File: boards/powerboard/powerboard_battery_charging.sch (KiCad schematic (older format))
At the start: 19 parts, among them P501 10k NTC, Q501 DMN6140L, Q502 PMV27UPE, Q503 IRF7343PBF, U501 LTC4010

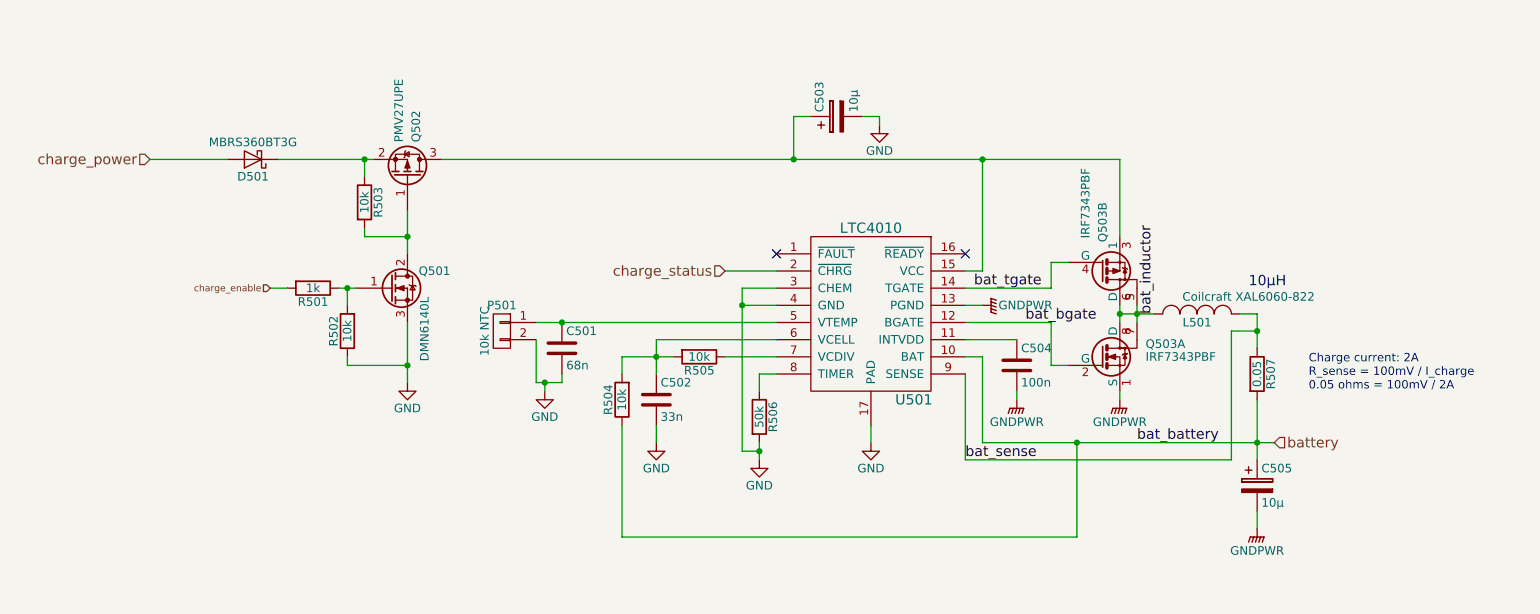
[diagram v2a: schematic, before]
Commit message: [powerboard] improve LTC4010
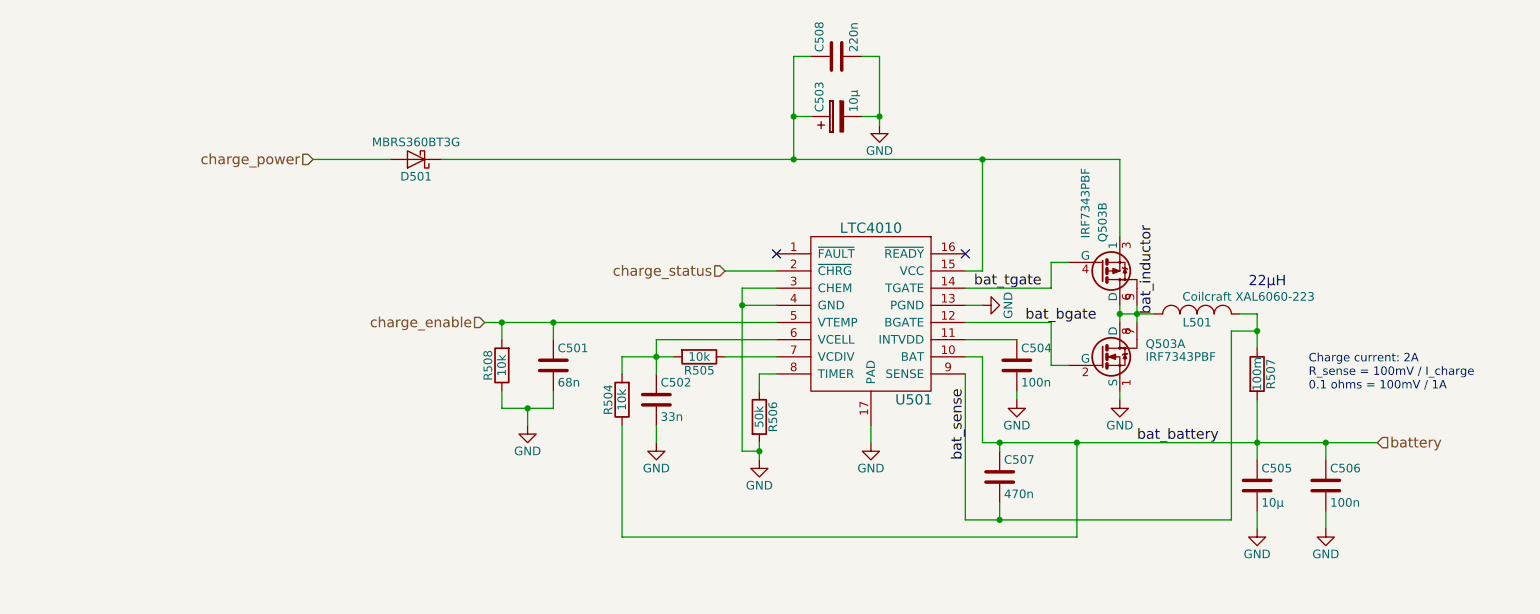
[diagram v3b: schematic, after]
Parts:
- removed C505: 10µ, Capacitors_SMD:C_0805, symbol CP
- removed P501: 10k NTC, Pin_Headers:Pin_Header_Straight_1x02_Pitch2.54mm, symbol CONN_01X02
- removed Q501: DMN6140L, TO_SOT_Packages_SMD:SOT-23, symbol Q_NMOS_GDS
- removed Q502: PMV27UPE, TO_SOT_Packages_SMD:SOT-23, symbol Q_PMOS_GSD
- removed R501: 1k, Resistors_SMD:R_0603, symbol R
- removed R502, R503: 10k, Resistors_SMD:R_0603, symbol R
- added C505: 10µ, symbol C
- added C506: 100n, symbol C
- added C507: 470n, symbol C
- added C508: 220n, symbol C
- added R508: 10k, Resistors_SMD:R_0603, symbol R
- L501: value Coilcraft XAL6060-822 -> Coilcraft XAL6060-223
- R507: value 0.05 -> 100m
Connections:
- net GNDPWR is gone; now on net GND: C504.2, Q503.1 (S), U501.13 (PGND)
- net GND: now also C505.2, C506.2, C508.2, R508.1
- net bat_sense: now also C507.2
- net battery: now also C505.1, C506.1, C507.1
- net charge_enable: now also C501.1, U501.5 (VTEMP), R508.2
- net at C503.1, Q503.3 (1), U501.15 (VCC): now also D501.1 (K), C508.1
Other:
- note added: "22µH"
- note added: "Charge current: 2A\nR_sense = 100mV / I_charge\n0.1 ohms = 100mV / 1A"
- note removed: "10µH"
- note removed: "Charge current: 2A\nR_sense = 100mV / I_charge\n0.05 ohms = 100mV / 2A"
- moved on the sheet: C501, D501

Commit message: [powerboard] LTC4010: fix R and C values
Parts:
- C502: value 33n -> 47n
- R504: value 10k -> 65k7
- R505: value 10k -> 8k2
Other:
- note added: "9 cells: R504 = 65.7k, R505 = 8.2k, R504/R505 = 8.01\n8 cells: R504 = 57.6k, R505 = 8.2k, R504/R505 = 7.02"
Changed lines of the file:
@@
 P 4950 3750
 F 0 "R505" V 5030 3750 50  0000 C CNN
-F 1 "10k" V 4950 3750 50  0000 C CNN
+F 1 "8k2" V 4950 3750 50  0000 C CNN
 F 2 "Resistors_SMD:R_0603" V 4880 3750 50  0001 C CNN
 F 3 "" H 4950 3750 50  0000 C CNN
@@
 P 4700 4000
 F 0 "C502" H 4725 4100 50  0000 L CNN
-F 1 "33n" H 4725 3900 50  0000 L CNN
+F 1 "47n" H 4725 3900 50  0000 L CNN
 F 2 "Capacitors_SMD:C_0603" H 4738 3850 50  0001 C CNN
 F 3 "" H 4700 4000 50  0000 C CNN
@@
 P 4500 4000
 F 0 "R504" V 4580 4000 50  0000 C CNN
-F 1 "10k" V 4500 4000 50  0000 C CNN
+F 1 "65k7" V 4500 4000 50  0000 C CNN
 F 2 "Resistors_SMD:R_0603" V 4430 4000 50  0001 C CNN
 F 3 "" H 4500 4000 50  0000 C CNN
@@
 	1    0    0    -1
 $EndComp
+Text Notes 4000 5150 0    60   ~ 0
+9 cells: R504 = 65.7k, R505 = 8.2k, R504/R505 = 8.01\n8 cells: R504 = 57.6k, R505 = 8.2k, R504/R505 = 7.02
 $EndSCHEMATC

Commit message: [powerboard] fix minor issues in all schematics; revision: rev10
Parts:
- C503: value 10µ -> 10µ 0805 35V
- C505: footprint (none) -> Capacitors_SMD:C_0805
- C506, C507, C508: footprint (none) -> Capacitors_SMD:C_0603
- D501: footprint Diodes_SMD:D_SMB_Handsoldering -> Diodes_SMD:D_SMB_Standard
- R507: footprint Resistors_SMD:R_1812_HandSoldering -> Resistors_SMD:R_1812
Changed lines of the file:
@@
 Sheet 4 11
 Title "Powerboard Battery Charging"
-Date "2017-03-15"
-Rev "20"
+Date "2017-11-23"
+Rev "rev10"
 Comp "VIPER"
 Comment1 ""
@@
 $EndComp
 $Comp
-L GND #PWR052
+L GND #PWR054
 U 1 1 58C99770
 P 3950 4150
-F 0 "#PWR052" H 3950 3900 50  0001 C CNN
+F 0 "#PWR054" H 3950 3900 50  0001 C CNN
 F 1 "GND" H 3950 4000 50  0000 C CNN
 F 2 "" H 3950 4150 50  0000 C CNN
@@
 $EndComp
 $Comp
-L GND #PWR053
+L GND #PWR055
 U 1 1 58C99B11
 P 5300 4350
-F 0 "#PWR053" H 5300 4100 50  0001 C CNN
+F 0 "#PWR055" H 5300 4100 50  0001 C CNN
 F 1 "GND" H 5300 4200 50  0000 C CNN
 F 2 "" H 5300 4350 50  0000 C CNN
@@
 F 0 "R507" V 8280 3850 50  0000 C CNN
 F 1 "100m" V 8200 3850 50  0000 C CNN
-F 2 "Resistors_SMD:R_1812_HandSoldering" V 8130 3850 50  0001 C CNN
+F 2 "Resistors_SMD:R_1812" V 8130 3850 50  0001 C CNN
 F 3 "" H 8200 3850 50  0000 C CNN
 	1    8200 3850
@@
 P 5750 2350
 F 0 "C503" H 5775 2450 50  0000 L CNN
-F 1 "10µ" H 5775 2250 50  0000 L CNN
+F 1 "10µ 0805 35V" V 5800 1700 50  0000 L CNN
 F 2 "Capacitors_SMD:C_0805" H 5788 2200 50  0001 C CNN
 F 3 "" H 5750 2350 50  0000 C CNN
@@
 Connection ~ 4700 3750
 $Comp
-L GND #PWR054
+L GND #PWR056
 U 1 1 58C9CC60
 P 4700 4250
-F 0 "#PWR054" H 4700 4000 50  0001 C CNN
+F 0 "#PWR056" H 4700 4000 50  0001 C CNN
 F 1 "GND" H 4700 4100 50  0000 C CNN
 F 2 "" H 4700 4250 50  0000 C CNN
@@
 Charge current: 2A\nR_sense = 100mV / I_charge\n0.1 ohms = 100mV / 1A
 $Comp
-L GND #PWR055
+L GND #PWR057
 U 1 1 58CF4775
 P 6000 2400
-F 0 "#PWR055" H 6000 2150 50  0001 C CNN
+F 0 "#PWR057" H 6000 2150 50  0001 C CNN
 F 1 "GND" H 6000 2250 50  0000 C CNN
 F 2 "" H 6000 2400 50  0000 C CNN
@@
 charge_enable
 $Comp
-L GND #PWR057
+L GND #PWR058
 U 1 1 58FD411A
 P 5950 4250
-F 0 "#PWR057" H 5950 4000 50  0001 C CNN
+F 0 "#PWR058" H 5950 4000 50  0001 C CNN
 F 1 "GND" H 5950 4100 50  0000 C CNN
 F 2 "" H 5950 4250 50  0000 C CNN
@@
 F 0 "D501" H 3300 2700 50  0000 C CNN
 F 1 "MBRS360BT3G" H 3300 2500 50  0000 C CNN
-F 2 "Diodes_SMD:D_SMB_Handsoldering" H 3300 2600 50  0001 C CNN
+F 2 "Diodes_SMD:D_SMB_Standard" H 3300 2600 50  0001 C CNN
 F 3 "" H 3300 2600 50  0001 C CNN
 	1    3300 2600
@@
 $EndComp
 $Comp
-L GND #PWR?
+L GND #PWR059
 U 1 1 5A144E32
 P 8200 4750
-F 0 "#PWR?" H 8200 4500 50  0001 C CNN
+F 0 "#PWR059" H 8200 4500 50  0001 C CNN
 F 1 "GND" H 8200 4600 50  0000 C CNN
 F 2 "" H 8200 4750 50  0000 C CNN
@@
 $EndComp
 $Comp
-L GND #PWR?
+L GND #PWR060
 U 1 1 5A144E6A
 P 7400 4000
-F 0 "#PWR?" H 7400 3750 50  0001 C CNN
+F 0 "#PWR060" H 7400 3750 50  0001 C CNN
 F 1 "GND" H 7400 3850 50  0000 C CNN
 F 2 "" H 7400 4000 50  0000 C CNN
@@
 $EndComp
 $Comp
-L GND #PWR?
+L GND #PWR061
 U 1 1 5A144EA2
 P 6800 4000
-F 0 "#PWR?" H 6800 3750 50  0001 C CNN
+F 0 "#PWR061" H 6800 3750 50  0001 C CNN
 F 1 "GND" H 6800 3850 50  0000 C CNN
 F 2 "" H 6800 4000 50  0000 C CNN
@@
 $EndComp
 $Comp
-L GND #PWR?
+L GND #PWR062
 U 1 1 5A14A095
 P 6600 3450
-F 0 "#PWR?" H 6600 3200 50  0001 C CNN
+F 0 "#PWR062" H 6600 3200 50  0001 C CNN
 F 1 "GND" H 6600 3300 50  0000 C CNN
 F 2 "" H 6600 3450 50  0000 C CNN
@@
 F 0 "C506" H 8625 4600 50  0000 L CNN
 F 1 "100n" H 8625 4400 50  0000 L CNN
-F 2 "" H 8638 4350 50  0001 C CNN
+F 2 "Capacitors_SMD:C_0603" H 8638 4350 50  0001 C CNN
 F 3 "" H 8600 4500 50  0001 C CNN
 	1    8600 4500
@@
 Connection ~ 8600 4250
 $Comp
-L GND #PWR?
+L GND #PWR063
 U 1 1 5A162449
 P 8600 4750
-F 0 "#PWR?" H 8600 4500 50  0001 C CNN
+F 0 "#PWR063" H 8600 4500 50  0001 C CNN
 F 1 "GND" H 8600 4600 50  0000 C CNN
 F 2 "" H 8600 4750 50  0000 C CNN
@@
 F 0 "C507" H 6725 4550 50  0000 L CNN
 F 1 "470n" H 6725 4350 50  0000 L CNN
-F 2 "" H 6738 4300 50  0001 C CNN
+F 2 "Capacitors_SMD:C_0603" H 6738 4300 50  0001 C CNN
 F 3 "" H 6700 4450 50  0001 C CNN
 	1    6700 4450
@@
 F 0 "C508" H 5775 2100 50  0000 L CNN
 F 1 "220n" H 5775 1900 50  0000 L CNN
-F 2 "" H 5788 1850 50  0001 C CNN
+F 2 "Capacitors_SMD:C_0603" H 5788 1850 50  0001 C CNN
 F 3 "" H 5750 2000 50  0001 C CNN
 	1    5750 2000
@@
 F 0 "C505" H 8225 4600 50  0000 L CNN
 F 1 "10µ" H 8225 4400 50  0000 L CNN
-F 2 "" H 8238 4350 50  0001 C CNN
+F 2 "Capacitors_SMD:C_0805" H 8238 4350 50  0001 C CNN
 F 3 "" H 8200 4500 50  0001 C CNN
 	1    8200 4500

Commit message: [powerboard] layout adjusted (wip)
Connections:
- net GND: no longer C505.2, C506.2
- new net GNDPWR: C505.2, C506.2
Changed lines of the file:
@@
 $Comp
 L GND #PWR059
-U 1 1 5A144E32
-P 8200 4750
-F 0 "#PWR059" H 8200 4500 50  0001 C CNN
-F 1 "GND" H 8200 4600 50  0000 C CNN
-F 2 "" H 8200 4750 50  0000 C CNN
-F 3 "" H 8200 4750 50  0000 C CNN
-	1    8200 4750
-	1    0    0    -1
-$EndComp
-$Comp
-L GND #PWR060
 U 1 1 5A144E6A
 P 7400 4000
-F 0 "#PWR060" H 7400 3750 50  0001 C CNN
+F 0 "#PWR059" H 7400 3750 50  0001 C CNN
 F 1 "GND" H 7400 3850 50  0000 C CNN
 F 2 "" H 7400 4000 50  0000 C CNN
@@
 $EndComp
 $Comp
-L GND #PWR061
+L GND #PWR060
 U 1 1 5A144EA2
 P 6800 4000
-F 0 "#PWR061" H 6800 3750 50  0001 C CNN
+F 0 "#PWR060" H 6800 3750 50  0001 C CNN
 F 1 "GND" H 6800 3850 50  0000 C CNN
 F 2 "" H 6800 4000 50  0000 C CNN
@@
 $EndComp
 $Comp
-L GND #PWR062
+L GND #PWR061
 U 1 1 5A14A095
 P 6600 3450
-F 0 "#PWR062" H 6600 3200 50  0001 C CNN
+F 0 "#PWR061" H 6600 3200 50  0001 C CNN
 F 1 "GND" H 6600 3300 50  0000 C CNN
 F 2 "" H 6600 3450 50  0000 C CNN
@@
 	8600 4250 8600 4350
 Connection ~ 8600 4250
-$Comp
-L GND #PWR063
-U 1 1 5A162449
-P 8600 4750
-F 0 "#PWR063" H 8600 4500 50  0001 C CNN
-F 1 "GND" H 8600 4600 50  0000 C CNN
-F 2 "" H 8600 4750 50  0000 C CNN
-F 3 "" H 8600 4750 50  0000 C CNN
-	1    8600 4750
-	1    0    0    -1
-$EndComp
 Wire Wire Line
 	8600 4750 8600 4650
@@
 Text Notes 4000 5150 0    60   ~ 0
 9 cells: R504 = 65.7k, R505 = 8.2k, R504/R505 = 8.01\n8 cells: R504 = 57.6k, R505 = 8.2k, R504/R505 = 7.02
+$Comp
+L GNDPWR #PWR062
+U 1 1 5A17A0A7
+P 8200 4750
+F 0 "#PWR062" H 8200 4550 50  0001 C CNN
+F 1 "GNDPWR" H 8200 4620 50  0000 C CNN
+F 2 "" H 8200 4700 50  0001 C CNN
+F 3 "" H 8200 4700 50  0001 C CNN
+	1    8200 4750
+	1    0    0    -1
+$EndComp
+$Comp
+L GNDPWR #PWR063
+U 1 1 5A17A0EF
+P 8600 4750
+F 0 "#PWR063" H 8600 4550 50  0001 C CNN
+F 1 "GNDPWR" H 8600 4620 50  0000 C CNN
+F 2 "" H 8600 4700 50  0001 C CNN
+F 3 "" H 8600 4700 50  0001 C CNN
+	1    8600 4750
+	1    0    0    -1
+$EndComp
 $EndSCHEMATC

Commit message: [powerboard] layout rev10; some changes to the schematic
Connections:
- net GNDPWR is gone; now on net GND: C505.2, C506.2
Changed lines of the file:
@@
 $EndComp
 $Comp
-L GND #PWR054
+L GND #PWR058
 U 1 1 58C99770
 P 3950 4150
-F 0 "#PWR054" H 3950 3900 50  0001 C CNN
+F 0 "#PWR058" H 3950 3900 50  0001 C CNN
 F 1 "GND" H 3950 4000 50  0000 C CNN
 F 2 "" H 3950 4150 50  0000 C CNN
@@
 $EndComp
 $Comp
-L GND #PWR055
+L GND #PWR059
 U 1 1 58C99B11
 P 5300 4350
-F 0 "#PWR055" H 5300 4100 50  0001 C CNN
+F 0 "#PWR059" H 5300 4100 50  0001 C CNN
 F 1 "GND" H 5300 4200 50  0000 C CNN
 F 2 "" H 5300 4350 50  0000 C CNN
@@
 Connection ~ 4700 3750
 $Comp
-L GND #PWR056
+L GND #PWR060
 U 1 1 58C9CC60
 P 4700 4250
-F 0 "#PWR056" H 4700 4000 50  0001 C CNN
+F 0 "#PWR060" H 4700 4000 50  0001 C CNN
 F 1 "GND" H 4700 4100 50  0000 C CNN
 F 2 "" H 4700 4250 50  0000 C CNN
@@
 Charge current: 2A\nR_sense = 100mV / I_charge\n0.1 ohms = 100mV / 1A
 $Comp
-L GND #PWR057
+L GND #PWR061
 U 1 1 58CF4775
 P 6000 2400
-F 0 "#PWR057" H 6000 2150 50  0001 C CNN
+F 0 "#PWR061" H 6000 2150 50  0001 C CNN
 F 1 "GND" H 6000 2250 50  0000 C CNN
 F 2 "" H 6000 2400 50  0000 C CNN
@@
 charge_enable
 $Comp
-L GND #PWR058
+L GND #PWR062
 U 1 1 58FD411A
 P 5950 4250
-F 0 "#PWR058" H 5950 4000 50  0001 C CNN
+F 0 "#PWR062" H 5950 4000 50  0001 C CNN
 F 1 "GND" H 5950 4100 50  0000 C CNN
 F 2 "" H 5950 4250 50  0000 C CNN
@@
 $EndComp
 $Comp
-L GND #PWR059
+L GND #PWR063
 U 1 1 5A144E6A
 P 7400 4000
-F 0 "#PWR059" H 7400 3750 50  0001 C CNN
+F 0 "#PWR063" H 7400 3750 50  0001 C CNN
 F 1 "GND" H 7400 3850 50  0000 C CNN
 F 2 "" H 7400 4000 50  0000 C CNN
@@
 $EndComp
 $Comp
-L GND #PWR060
+L GND #PWR064
 U 1 1 5A144EA2
 P 6800 4000
-F 0 "#PWR060" H 6800 3750 50  0001 C CNN
+F 0 "#PWR064" H 6800 3750 50  0001 C CNN
 F 1 "GND" H 6800 3850 50  0000 C CNN
 F 2 "" H 6800 4000 50  0000 C CNN
@@
 $EndComp
 $Comp
-L GND #PWR061
+L GND #PWR065
 U 1 1 5A14A095
 P 6600 3450
-F 0 "#PWR061" H 6600 3200 50  0001 C CNN
+F 0 "#PWR065" H 6600 3200 50  0001 C CNN
 F 1 "GND" H 6600 3300 50  0000 C CNN
 F 2 "" H 6600 3450 50  0000 C CNN
@@
 9 cells: R504 = 65.7k, R505 = 8.2k, R504/R505 = 8.01\n8 cells: R504 = 57.6k, R505 = 8.2k, R504/R505 = 7.02
 $Comp
-L GNDPWR #PWR062
-U 1 1 5A17A0A7
+L GND #PWR066
+U 1 1 5A1B3B71
 P 8200 4750
-F 0 "#PWR062" H 8200 4550 50  0001 C CNN
-F 1 "GNDPWR" H 8200 4620 50  0000 C CNN
-F 2 "" H 8200 4700 50  0001 C CNN
-F 3 "" H 8200 4700 50  0001 C CNN
+F 0 "#PWR066" H 8200 4500 50  0001 C CNN
+F 1 "GND" H 8200 4600 50  0000 C CNN
+F 2 "" H 8200 4750 50  0000 C CNN
+F 3 "" H 8200 4750 50  0000 C CNN
 	1    8200 4750
 	1    0    0    -1
 $EndComp
 $Comp
-L GNDPWR #PWR063
-U 1 1 5A17A0EF
+L GND #PWR067
+U 1 1 5A1B3BB2
 P 8600 4750
-F 0 "#PWR063" H 8600 4550 50  0001 C CNN
-F 1 "GNDPWR" H 8600 4620 50  0000 C CNN
-F 2 "" H 8600 4700 50  0001 C CNN
-F 3 "" H 8600 4700 50  0001 C CNN
+F 0 "#PWR067" H 8600 4500 50  0001 C CNN
+F 1 "GND" H 8600 4600 50  0000 C CNN
+F 2 "" H 8600 4750 50  0000 C CNN
+F 3 "" H 8600 4750 50  0000 C CNN
 	1    8600 4750
 	1    0    0    -1
